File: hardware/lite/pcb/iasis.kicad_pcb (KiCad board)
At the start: 6 copper layers, 125 x 89 mm, 718 parts, among them J1001 USB4105-GF-A-120, J1101 SWD debug, J1131 SM04B-SRSS-TB, J1132 UART debug, J2001 05A20L24P, J401 1054500101, J501 1054500101, J601 1054500101, J701 1054500101, J801 1054500101, J901 1054500101, Q1001 SP60N05GNJ, Q1002 SP60N05GNJ, Q1003 2N7002, Q1004 2N7002, Q1005 2N7002, Q1221 2N7002, Q1230 TMGN4060DF, Q1231 TMGN4060DF, Q1232 SP60N05GNJ, Q1233 SP60N05GNJ, Q1234 2N7002, Q1321 2N7002, Q1330 TMGN4060DF, Q1331 TMGN4060DF, Q1332 SP60N05GNJ, Q1333 SP60N05GNJ, Q1334 2N7002, Q1421 2N7002, Q1430 TMGN4060DF, Q1431 TMGN4060DF, Q1432 SP60N05GNJ, Q1433 SP60N05GNJ, Q1434 2N7002, Q1521 2N7002, Q1530 TMGN4060DF, Q1531 TMGN4060DF, Q1532 SP60N05GNJ, Q1533 SP60N05GNJ, Q1534 2N7002, Q1621 2N7002, Q1630 TMGN4060DF, Q1631 TMGN4060DF, Q1632 SP60N05GNJ, Q1633 SP60N05GNJ, Q1634 2N7002, Q1911 2N7002, Q1912 2N7002, Q901 2N7002, Q902 2N7002, SW1101 PTS645SL50SMTR92LFS, SW1102 PTS645SL50SMTR92LFS, SW1171 PTS645SL50SMTR92LFS, U1001 LM74502DDFR, U1002 CH224Q, U1003 TPS26600PWPR, U1004 LMR51450SDRRR, U1005 TPS259470ARPWR, U1040 AP3441SHE-7B, U1060 AP3441SHE-7B, U1080 TPS3808G33DBVR, U1101 RP2354B, U1131 TCA9548APWR, U1141 TMUX1511PWR, U1142 TMUX1511PWR, U1171 SN74AHCT1G125DBVR, U1172 TCA6408ARGTR, U1181 74HC595D,118, U1182 74HC595D,118, U1202 TPS259470ARPWR, U1203 74LVC2G08DC-Q100H, U1230 TPS55288RPMR, U1231 LM74502DDFR, U1302 TPS259470ARPWR, U1303 74LVC2G08DC-Q100H, U1330 TPS55288RPMR, U1331 LM74502DDFR, U1402 TPS259470ARPWR, U1403 74LVC2G08DC-Q100H, U1430 TPS55288RPMR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

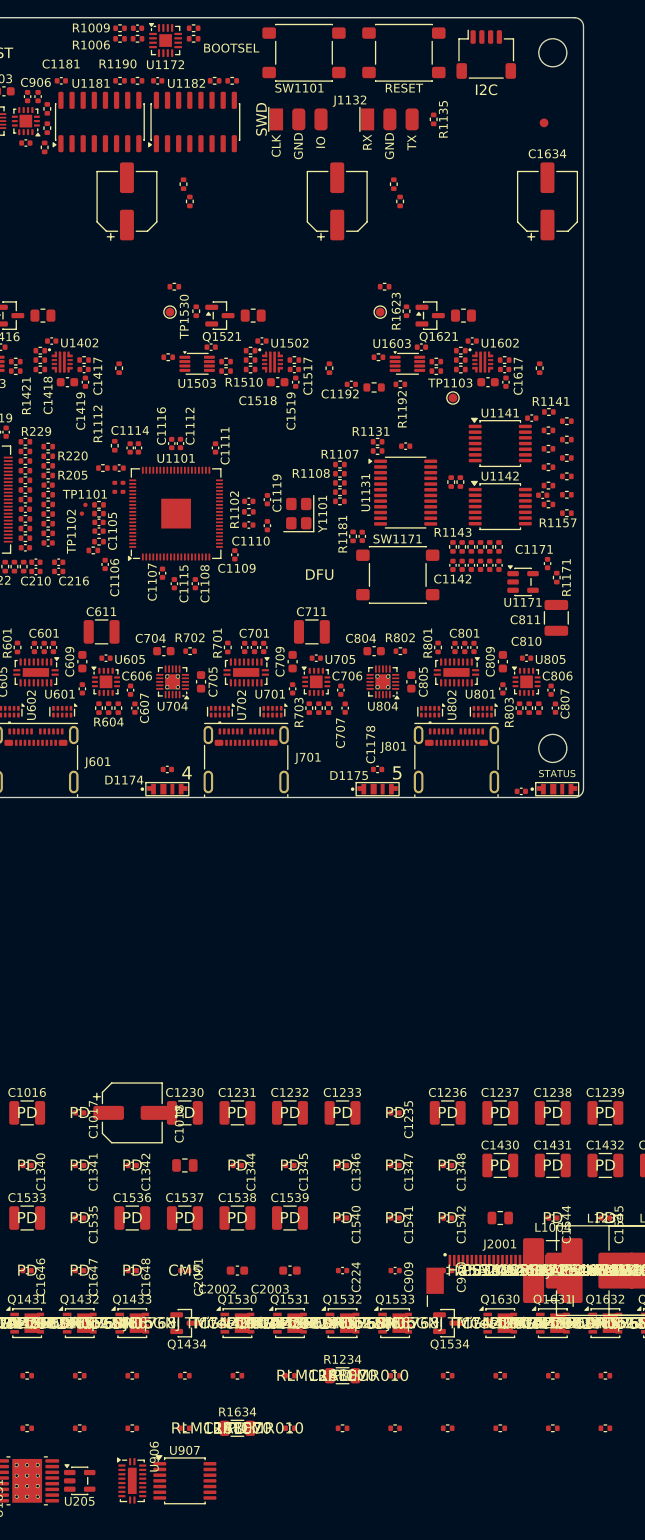
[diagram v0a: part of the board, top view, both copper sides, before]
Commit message: feat(hardware): use smaller mux, I2C switch, 595 and button packages
The TMUX1511s move to UQFN-16 (RSV), the TCA9548A to VQFN-24 (RGE),
the 74HC595s to TSSOP-16 and the BOOTSEL and RESET buttons to the
Omron B3U, which frees about 300 mm2 of the middle band. The case
button keeps the PTS645.
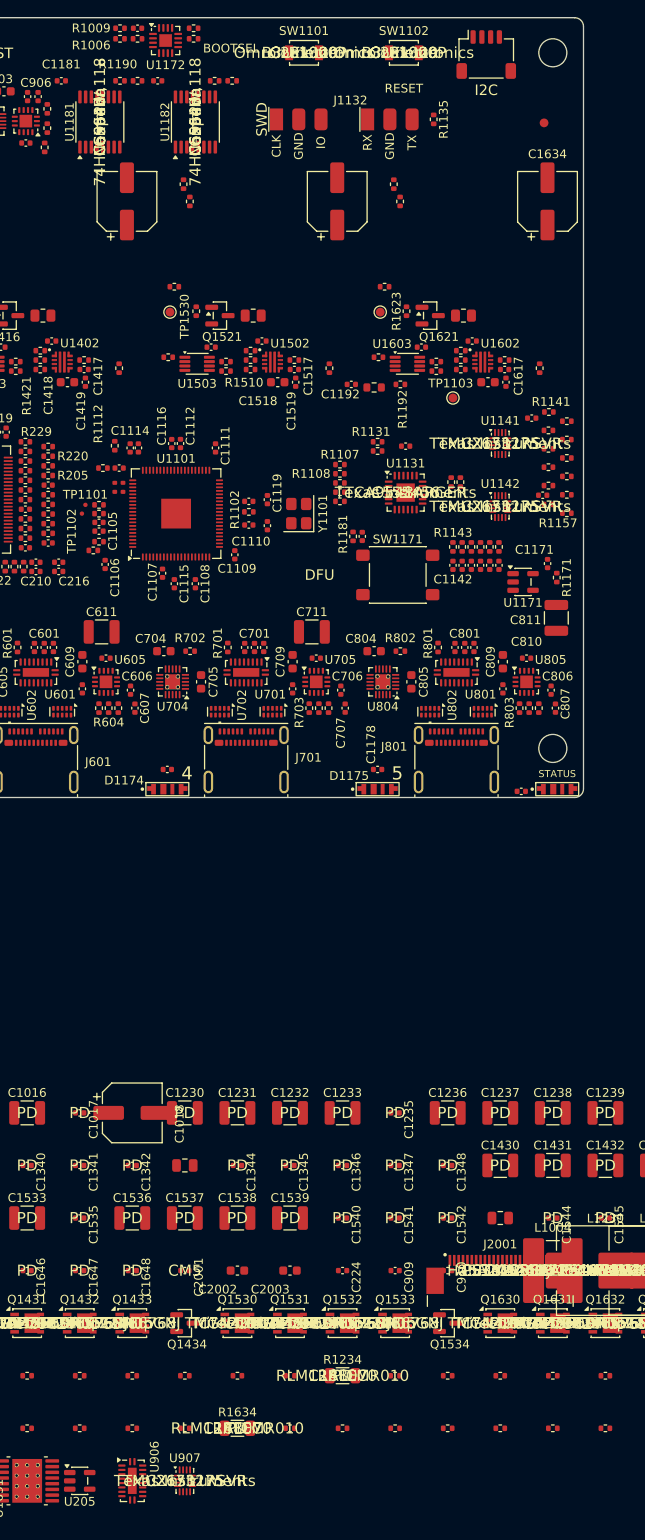
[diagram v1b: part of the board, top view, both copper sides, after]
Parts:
- SW1101, SW1102: value PTS645SL50SMTR92LFS -> B3U-1000P; footprint Button_Switch_SMD:SW_SPST_PTS645Sx43SMTR92 -> Button_Switch_SMD:SW_SPST_B3U-1000P
- U1131: value TCA9548APWR -> TCA9548ARGER; footprint Package_SO:TSSOP-24_4.4x7.8mm_P0.65mm -> Package_DFN_QFN:Texas_RGE0024C_VQFN-24-1EP_4x4mm_P0.5mm_EP2.1x2.1mm
- U1141, U1142, U907: value TMUX1511PWR -> TMUX1511RSVR; footprint Package_SO:TSSOP-14_4.4x5mm_P0.65mm -> Package_DFN_QFN:UQFN-16_1.8x2.6mm_P0.4mm
- U1181, U1182: value 74HC595D,118 -> 74HC595PW; footprint Package_SO:SOIC-16_3.9x9.9mm_P1.27mm -> Package_SO:TSSOP-16_4.4x5mm_P0.65mm
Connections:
- U1131 pad 1: GND -> P1_SDA
- U1131 pad 10: P4_SDA -> P5_SDA
- U1131 pad 11: P4_SCL -> P5_SCL
- U1131 pad 12: GND -> EXT_SDA
- U1131 pad 13: P5_SDA -> EXT_SCL
- U1131 pad 14: P5_SCL -> HUB_SDA
- U1131 pad 15: EXT_SDA -> HUB_SCL
- U1131 pad 16: EXT_SCL -> AUX_SDA
- U1131 pad 17: HUB_SDA -> AUX_SCL
- U1131 pad 18: HUB_SCL -> GND
- U1131 pad 19: AUX_SDA -> MCU_I2C_SCL
- U1131 pad 2: GND -> P1_SCL
- U1131 pad 20: AUX_SCL -> MCU_I2C_SDA
- U1131 pad 21: GND -> 3V3_AON
- U1131 pad 22: MCU_I2C_SCL -> GND
- U1131 pad 23: MCU_I2C_SDA -> GND
- U1131 pad 24: 3V3_AON -> AON_RESET_N
- U1131 pad 3: AON_RESET_N -> P2_SDA
- U1131 pad 4: P1_SDA -> P2_SCL
- U1131 pad 5: P1_SCL -> P3_SDA
- U1131 pad 6: P2_SDA -> P3_SCL
- U1131 pad 7: P2_SCL -> P4_SDA
- U1131 pad 8: P3_SDA -> P4_SCL
- U1131 pad 9: P3_SCL -> GND
- U1141 pad 10: AON_RESET_N -> /Port voltage measurement/LOCAL_P3_DIV
- U1141 pad 11: P4_VBUS_ADC -> AON_RESET_N
- U1141 pad 12: /Port voltage measurement/LOCAL_P4_DIV -> unconnected-(U1141-NC-Pad12)
- U1141 pad 13: AON_RESET_N -> P4_VBUS_ADC
- U1141 pad 14: 3V3_AON -> /Port voltage measurement/LOCAL_P4_DIV
- U1141 pad 7: GND -> unconnected-(U1141-NC-Pad7)
- U1141 pad 8: P3_VBUS_ADC -> GND
- U1141 pad 9: /Port voltage measurement/LOCAL_P3_DIV -> P3_VBUS_ADC
- U1142 pad 12: GND -> unconnected-(U1142-NC-Pad12)
- U1142 pad 14: 3V3_AON -> GND
- U1142 pad 7: GND -> unconnected-(U1142-NC-Pad7)
- U907 pad 10: /Host port/CM5_HOST_N -> EXT_D_P
- U907 pad 11: HUB_D_N -> /Host port/CM5_HOST_N
- U907 pad 12: EXT_D_N -> unconnected-(U907-NC-Pad12)
- U907 pad 13: /Host port/CM5_HOST_N -> HUB_D_N
- U907 pad 14: 3V3_AON -> EXT_D_N
- U907 pad 7: GND -> unconnected-(U907-NC-Pad7)
- U907 pad 8: HUB_D_P -> GND
- U907 pad 9: EXT_D_P -> HUB_D_P

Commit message: fix(hardware): put the hub and side-link lanes in USB_90
The hub upstream and CM5 side-link nets (HUB_ and SIDE_ TX, RX and D)
were left in the default class when the side link was added. A rule
lets the TMUX1511's corner pads keep their 0.15 mm package spacing
inside the class clearance.

U907 now carries D- on channel 1 and D+ on channel 2, the reverse of
channels 3 and 4, so each HUB_D net joins neighbouring pins around the
RSV package and its four-pin tie needs no via.
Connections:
- U907 pad 2: SIDE_D_P -> SIDE_D_N
- U907 pad 3: HUB_D_P -> HUB_D_N
- U907 pad 5: SIDE_D_N -> SIDE_D_P
- U907 pad 6: HUB_D_N -> HUB_D_P
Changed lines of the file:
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@@
 			(layers "F.Cu" "F.Mask" "F.Paste")
 			(roundrect_rratio 0.25)
-			(net "SIDE_D_P")
+			(net "SIDE_D_N")
 			(pinfunction "S1_2")
 			(pintype "bidirectional")
@@
 			(layers "F.Cu" "F.Mask" "F.Paste")
 			(roundrect_rratio 0.25)
-			(net "HUB_D_P")
+			(net "HUB_D_N")
 			(pinfunction "D1_3")
 			(pintype "bidirectional")
@@
 			(layers "F.Cu" "F.Mask" "F.Paste")
 			(roundrect_rratio 0.25)
-			(net "SIDE_D_N")
+			(net "SIDE_D_P")
 			(pinfunction "S2_5")
 			(pintype "bidirectional")
@@
 			(layers "F.Cu" "F.Mask" "F.Paste")
 			(roundrect_rratio 0.25)
-			(net "HUB_D_N")
+			(net "HUB_D_P")
 			(pinfunction "D2_6")
 			(pintype "bidirectional")

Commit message: fix(hardware): swap the host-select mux channels
The hub's upstream pins read RX before TX, the reverse of the
HD3SS3212's channel order, so U906 now carries RX on channel 0 and TX
on channel 1 at all three ports. The hub and side-link pairs reach it
without crossing; the J901 path keeps the one crossing its pin orders
require, in the run to U903, which stays in step with the target-port
muxes.
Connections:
- U906 pad 12: SIDE_RX_N -> SIDE_TX_N
- U906 pad 13: SIDE_RX_P -> SIDE_TX_P
- U906 pad 14: SIDE_TX_N -> SIDE_RX_N
- U906 pad 15: SIDE_TX_P -> SIDE_RX_P
- U906 pad 16: EXT_RX_N -> EXT_TX_N
- U906 pad 17: EXT_RX_P -> EXT_TX_P
- U906 pad 18: EXT_TX_N -> EXT_RX_N
- U906 pad 19: EXT_TX_P -> EXT_RX_P
- U906 pad 3: HUB_TX_P -> HUB_RX_P
- U906 pad 4: HUB_TX_N -> HUB_RX_N
- U906 pad 7: HUB_RX_P -> HUB_TX_P
- U906 pad 8: HUB_RX_N -> HUB_TX_N
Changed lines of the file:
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@@
 			(layers "F.Cu" "F.Mask" "F.Paste")
 			(roundrect_rratio 0.25)
-			(net "HUB_TX_P")
+			(net "HUB_RX_P")
 			(pinfunction "A0P_3")
 			(pintype "passive")
@@
 			(layers "F.Cu" "F.Mask" "F.Paste")
 			(roundrect_rratio 0.25)
-			(net "HUB_TX_N")
+			(net "HUB_RX_N")
 			(pinfunction "A0N_4")
 			(pintype "passive")
@@
 			(layers "F.Cu" "F.Mask" "F.Paste")
 			(roundrect_rratio 0.25)
-			(net "HUB_RX_P")
+			(net "HUB_TX_P")
 			(pinfunction "A1P_7")
 			(pintype "passive")
@@
 			(layers "F.Cu" "F.Mask" "F.Paste")
 			(roundrect_rratio 0.25)
-			(net "HUB_RX_N")
+			(net "HUB_TX_N")
 			(pinfunction "A1N_8")
 			(pintype "passive")
@@
 			(layers "F.Cu" "F.Mask" "F.Paste")
 			(roundrect_rratio 0.25)
-			(net "SIDE_RX_N")
+			(net "SIDE_TX_N")
 			(pinfunction "C1N_12")
 			(pintype "passive")
@@
 			(layers "F.Cu" "F.Mask" "F.Paste")
 			(roundrect_rratio 0.25)
-			(net "SIDE_RX_P")
+			(net "SIDE_TX_P")
 			(pinfunction "C1P_13")
 			(pintype "passive")
@@
 			(layers "F.Cu" "F.Mask" "F.Paste")
 			(roundrect_rratio 0.25)
-			(net "SIDE_TX_N")
+			(net "SIDE_RX_N")
 			(pinfunction "C0N_14")
 			(pintype "passive")
@@
 			(layers "F.Cu" "F.Mask" "F.Paste")
 			(roundrect_rratio 0.25)
-			(net "SIDE_TX_P")
+			(net "SIDE_RX_P")
 			(pinfunction "C0P_15")
 			(pintype "passive")
@@
 			(layers "F.Cu" "F.Mask" "F.Paste")
 			(roundrect_rratio 0.25)
-			(net "EXT_RX_N")
+			(net "EXT_TX_N")
 			(pinfunction "B1N_16")
 			(pintype "passive")
@@
 			(layers "F.Cu" "F.Mask" "F.Paste")
 			(roundrect_rratio 0.25)
-			(net "EXT_RX_P")
+			(net "EXT_TX_P")
 			(pinfunction "B1P_17")
 			(pintype "passive")
@@
 			(layers "F.Cu" "F.Mask" "F.Paste")
 			(roundrect_rratio 0.25)
-			(net "EXT_TX_N")
+			(net "EXT_RX_N")
 			(pinfunction "B0N_18")
 			(pintype "passive")
@@
 			(layers "F.Cu" "F.Mask" "F.Paste")
 			(roundrect_rratio 0.25)
-			(net "EXT_TX_P")
+			(net "EXT_RX_P")
 			(pinfunction "B0P_19")
 			(pintype "passive")
